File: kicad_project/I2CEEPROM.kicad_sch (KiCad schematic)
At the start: 3 parts, among them U15 24FC64-I/SN

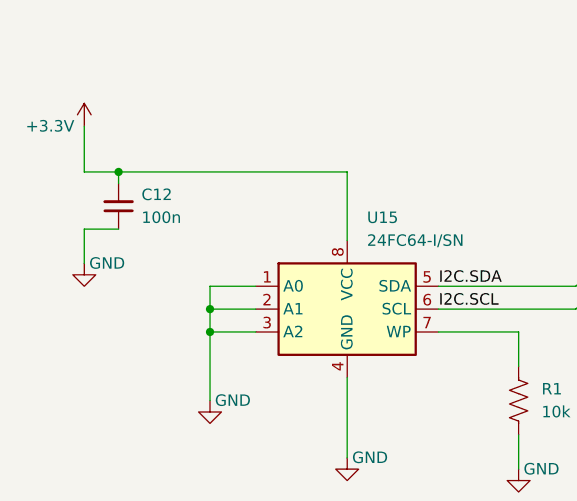
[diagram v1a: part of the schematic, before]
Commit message: Add part numbers for capacitors, start working on BoM job
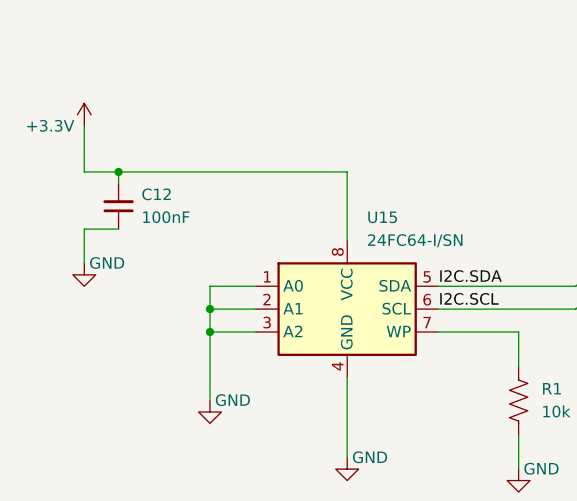
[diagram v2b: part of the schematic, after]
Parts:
- C12: value 100n -> 100nF; LibRef (none) -> GRM319R72A104KA01D; Supplier (none) -> Digi-Key
- R1, U15: Supplier (none) -> Digi-Key
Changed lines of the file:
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@@
+      (effects (font (size 1.27 1.27)) hide)
+    )
+    (property "Supplier" "Digi-Key" (at 111.76 78.74 0)
+      (effects (font (size 1.27 1.27)) hide)
+    )
+    (property "LibRef" "" (at 111.76 78.74 0)
       (effects (font (size 1.27 1.27)) hide)
     )
@@
       (effects (font (size 1.27 1.27)) (justify right))
     )
-    (property "Value" "100n" (at 69.85 58.4136 0)
+    (property "Value" "100nF" (at 69.85 58.4136 0)
       (effects (font (size 1.27 1.27)) (justify right))
     )
@@
     )
     (property "Datasheet" "~" (at 67.31 57.15 0)
+      (effects (font (size 1.27 1.27)) hide)
+    )
+    (property "SKU" "" (at 67.31 57.15 0)
+      (effects (font (size 1.27 1.27)) hide)
+    )
+    (property "Supplier" "Digi-Key" (at 67.31 57.15 0)
+      (effects (font (size 1.27 1.27)) hide)
+    )
+    (property "LibRef" "GRM319R72A104KA01D" (at 67.31 57.15 0)
       (effects (font (size 1.27 1.27)) hide)
     )
@@
       (effects (font (size 1.27 1.27)) hide)
     )
+    (property "Supplier" "Digi-Key" (at 92.71 68.58 0)
+      (effects (font (size 1.27 1.27)) hide)
+    )
+    (property "LibRef" "" (at 92.71 68.58 0)
+      (effects (font (size 1.27 1.27)) hide)
+    )

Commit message: Fill in all part numbers, add pcbinv bom job
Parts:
- R1: LibRef (none) -> ERJ-8ENF1002V; SKU (none) -> P10.0KFCT-ND
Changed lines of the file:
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@@
       (effects (font (size 1.27 1.27)) hide)
     )
-    (property "LibRef" "" (at 111.76 78.74 0)
+    (property "LibRef" "ERJ-8ENF1002V" (at 111.76 78.74 0)
       (effects (font (size 1.27 1.27)) hide)
     )
+    (property "SKU" "P10.0KFCT-ND" (at 111.76 78.74 0)
+      (effects (font (size 1.27 1.27)) hide)
+    )

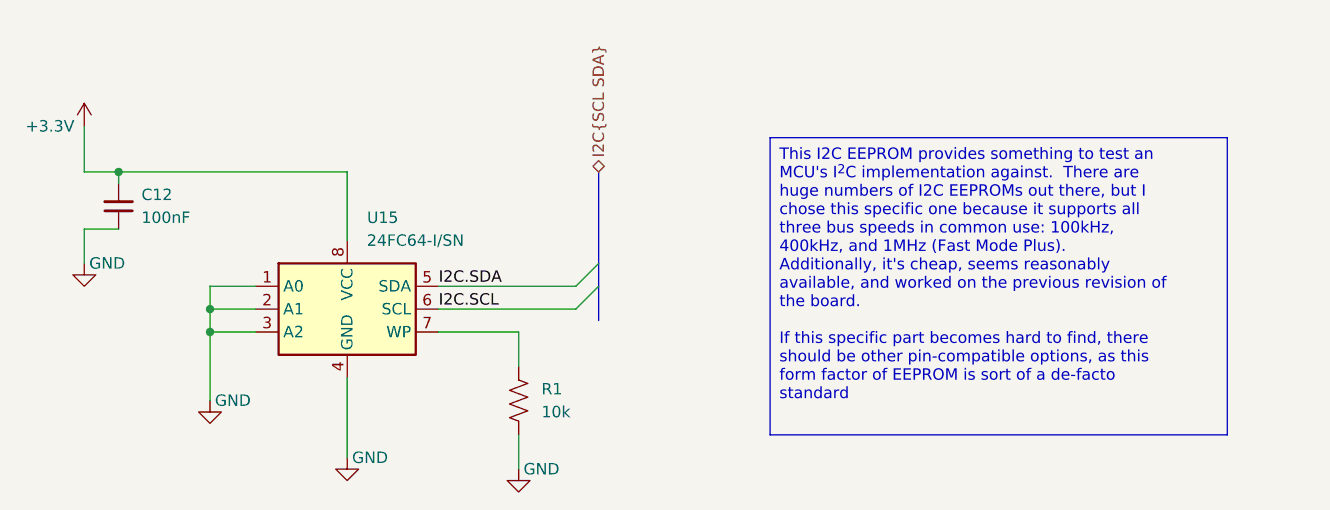
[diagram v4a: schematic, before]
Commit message: Update to KiCAD 8, start adding CAN transceiver
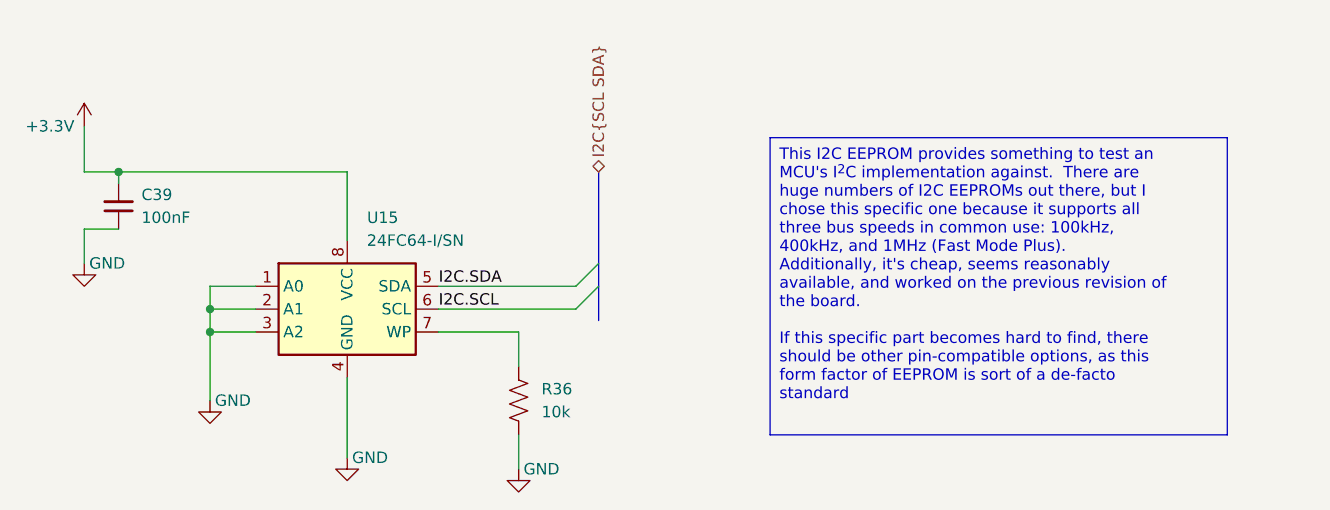
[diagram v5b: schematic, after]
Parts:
- renumbered C12 to C39, R1 to R36
